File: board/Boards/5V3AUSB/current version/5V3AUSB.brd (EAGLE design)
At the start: 36.8 x 51.7 mm, 18 parts

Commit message: updates to 5V 3A board
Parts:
- moved D1 3.81 mm to (35.6, 24.1)
- moved L1 3.81 mm to (27.9, 22.9)
- moved R1 2.84 mm to (33.0, 41.9)
- moved C2 2.54 mm to (16.5, 14.0)
- moved TP3 2.54 mm to (34.3, 8.89)
- moved R2 1.27 mm to (16.5, 7.62)
- moved R4 1.27 mm to (16.5, 2.54)
- moved LED1 1.27 mm to (25.4, 40.6)
- moved R3 1.27 mm to (16.5, 5.08)
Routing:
- net N$2: track 17.8 -> 21.2 mm
- net GND: track 17.5 -> 20.0 mm
- net N$5: track 3.18 -> 4.63 mm
- net N$3: track 7.55 -> 8.82 mm
- net N$6: track 12.0 -> 12.6 mm
- net N$7: track 11.8 -> 12.3 mm
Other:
- board size 36.8 x 51.7 mm -> 39.4 x 51.7 mm
- board text added: "5V 3A USB Power V1.1 C.G & D.K hitchBOT Dec 2014"
- board text removed: "5V 3A USB Power V1.0 C.G & D.K hitchBOT August 2014"

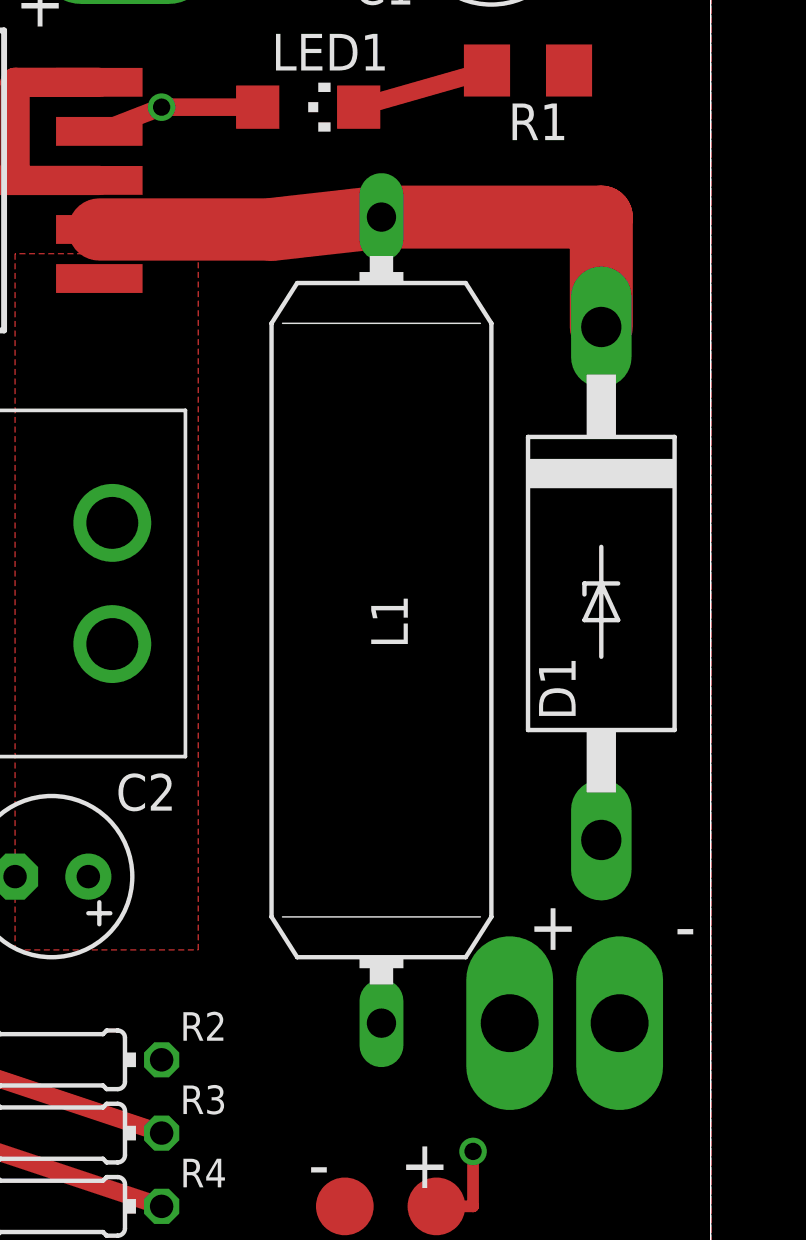
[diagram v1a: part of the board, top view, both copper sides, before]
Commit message: fixed text location as per conflict on OSH park
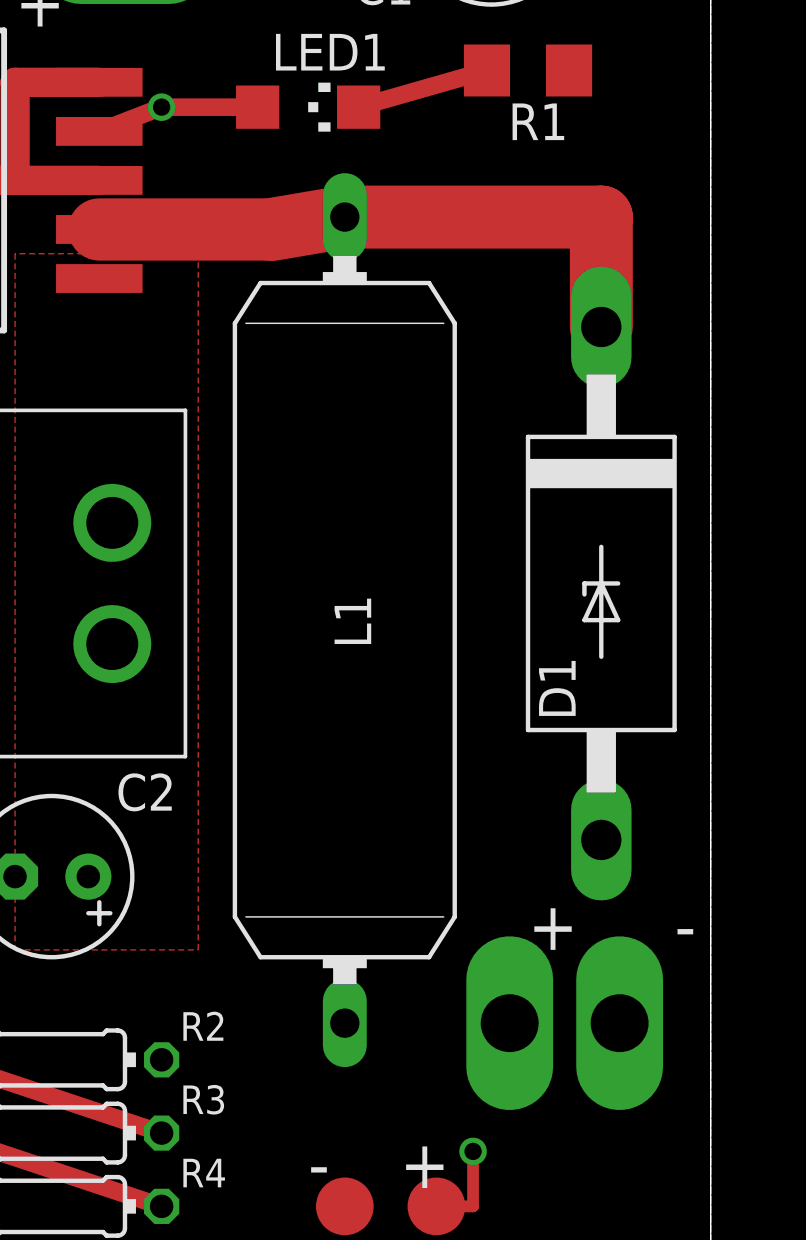
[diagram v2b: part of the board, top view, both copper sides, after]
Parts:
- moved L1 1.27 mm to (26.7, 22.9)
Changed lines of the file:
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@@
 <text x="38.1" y="11.43" size="1.6764" layer="21">-</text>
 <text x="25.4" y="3.175" size="1.6764" layer="21">-</text>
-<text x="20.32" y="20.32" size="1.6764" layer="22" rot="MR90">5V 3A
+<text x="22.86" y="20.32" size="1.6764" layer="22" rot="MR90">5V 3A
 USB Power V1.1
 C.G &amp; D.K
@@
 <attribute name="NAME" x="33.401" y="21.59" size="1.27" layer="25" ratio="10" rot="R270"/>
 </element>
-<element name="L1" library="inductors" package="SUKW3-27" value="22uH" x="27.94" y="22.86" smashed="yes" rot="R270">
-<attribute name="NAME" x="27.5844" y="23.749" size="1.27" layer="25" ratio="10" rot="R270"/>
-<attribute name="VALUE" x="27.2288" y="30.607" size="1.27" layer="27" ratio="10" rot="R270"/>
+<element name="L1" library="inductors" package="SUKW3-27" value="22uH" x="26.67" y="22.86" smashed="yes" rot="R270">
+<attribute name="NAME" x="26.3144" y="23.749" size="1.27" layer="25" ratio="10" rot="R270"/>
+<attribute name="VALUE" x="25.9588" y="30.607" size="1.27" layer="27" ratio="10" rot="R270"/>
 </element>
 <element name="TO265-5" library="on-semiconductor" package="TO263_5" value="CAT4101" x="10.16" y="38.1" smashed="yes" rot="R90">
@@
 <contactref element="TO265-5" pad="2"/>
 <wire x1="18.16" y1="36.4" x2="24.13" y2="36.4" width="2.159" layer="1"/>
-<wire x1="24.13" y1="36.4" x2="27.94" y2="36.83" width="2.1844" layer="1"/>
-<wire x1="27.94" y1="36.83" x2="35.56" y2="36.83" width="2.1844" layer="1"/>
+<wire x1="24.13" y1="36.4" x2="26.67" y2="36.83" width="2.1844" layer="1"/>
+<wire x1="26.67" y1="36.83" x2="35.56" y2="36.83" width="2.1844" layer="1"/>
 <wire x1="35.56" y1="36.83" x2="35.56" y2="33.02" width="2.1844" layer="1"/>
 </signal>
